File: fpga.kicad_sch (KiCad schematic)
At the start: 32 parts, among them J301 program, U301 ICE40HX8K-BG121, U302 W25Q32JVSS, Y301 50Mhz, Y302 12Mhz

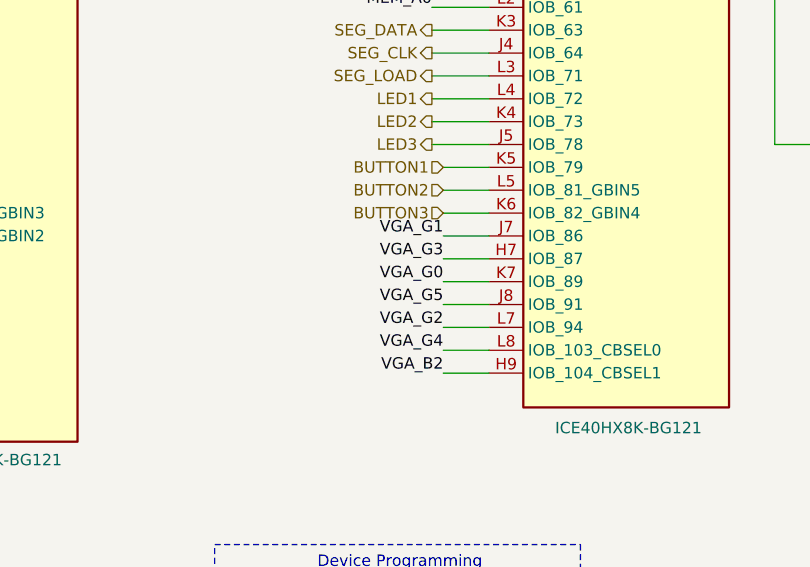
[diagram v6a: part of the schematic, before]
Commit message: Additional routing
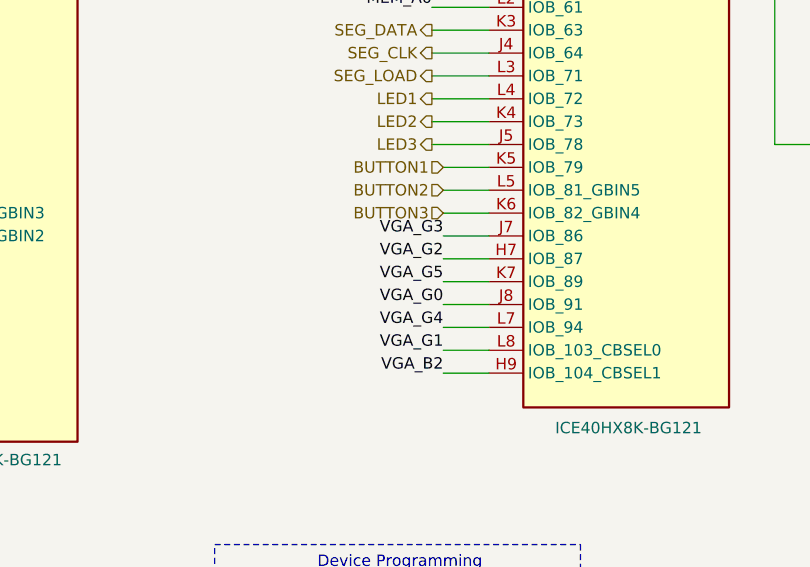
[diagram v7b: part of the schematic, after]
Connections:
- net VGA_G0: now also U301.J8 (IOB_91); no longer U301.K7 (IOB_89)
- net VGA_G1: now also U301.L8 (IOB_103_CBSEL0); no longer U301.J7 (IOB_86)
- net VGA_G2: now also U301.H7 (IOB_87); no longer U301.L7 (IOB_94)
- net VGA_G3: now also U301.J7 (IOB_86); no longer U301.H7 (IOB_87)
- net VGA_G4: now also U301.L7 (IOB_94); no longer U301.L8 (IOB_103_CBSEL0)
- net VGA_G5: now also U301.K7 (IOB_89); no longer U301.J8 (IOB_91)
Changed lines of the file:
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@@
 	)
 	(label "VGA_G5"
-		(at 166.37 78.74 180)
+		(at 166.37 76.2 180)
 		(effects
 			(font
@@
 	)
 	(label "VGA_G4"
-		(at 166.37 83.82 180)
+		(at 166.37 81.28 180)
 		(effects
 			(font
@@
 	)
 	(label "VGA_G0"
-		(at 166.37 76.2 180)
+		(at 166.37 78.74 180)
 		(effects
 			(font
@@
 	)
 	(label "VGA_G2"
-		(at 166.37 81.28 180)
+		(at 166.37 73.66 180)
 		(effects
 			(font
@@
 	)
 	(label "VGA_G3"
-		(at 166.37 73.66 180)
+		(at 166.37 71.12 180)
 		(effects
 			(font
@@
 	)
 	(label "VGA_G1"
-		(at 166.37 71.12 180)
-		(effects
-			(font
+		(at 166.37 83.82 180)
+		(effects
+			(font

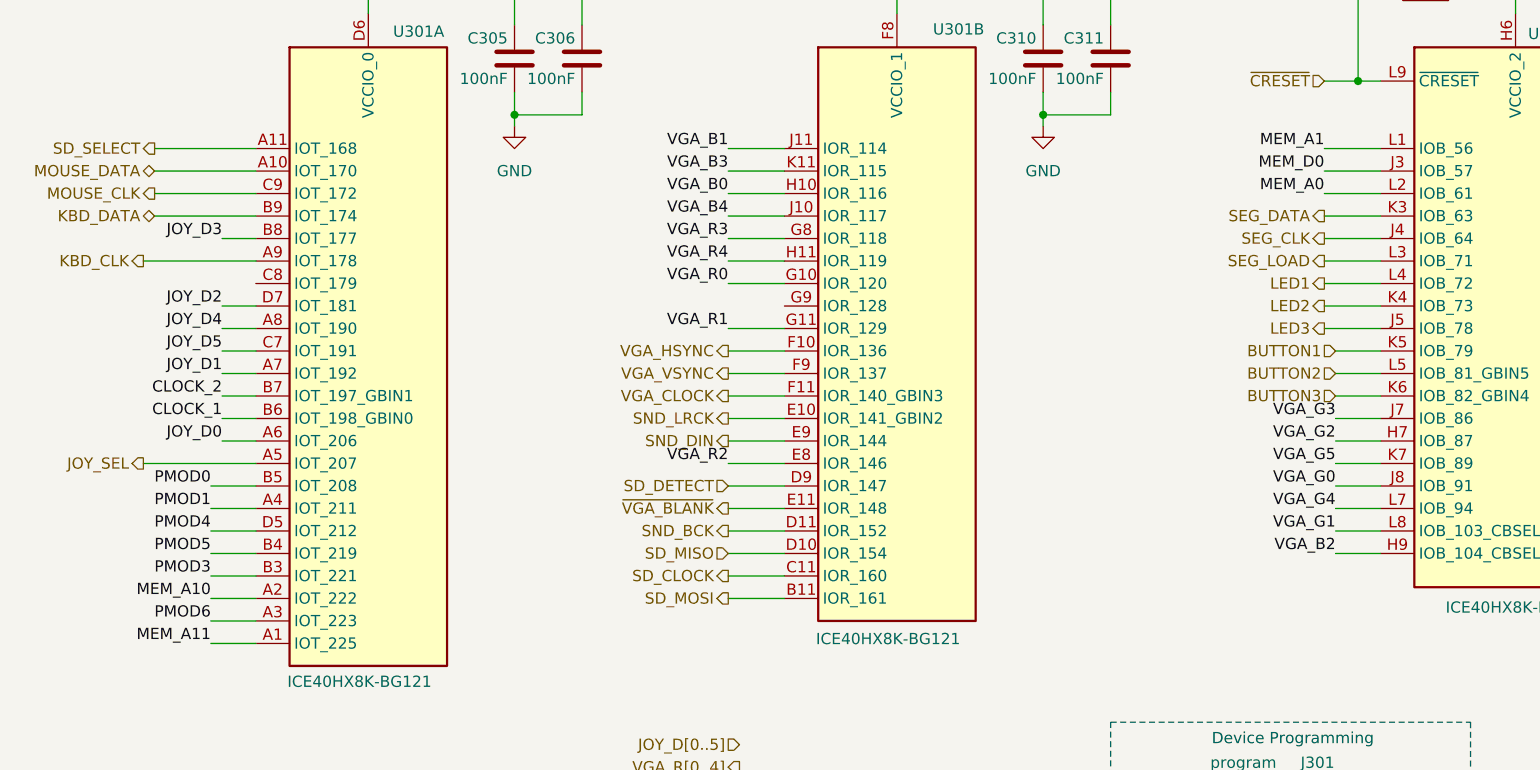
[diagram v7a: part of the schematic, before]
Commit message: More layout done
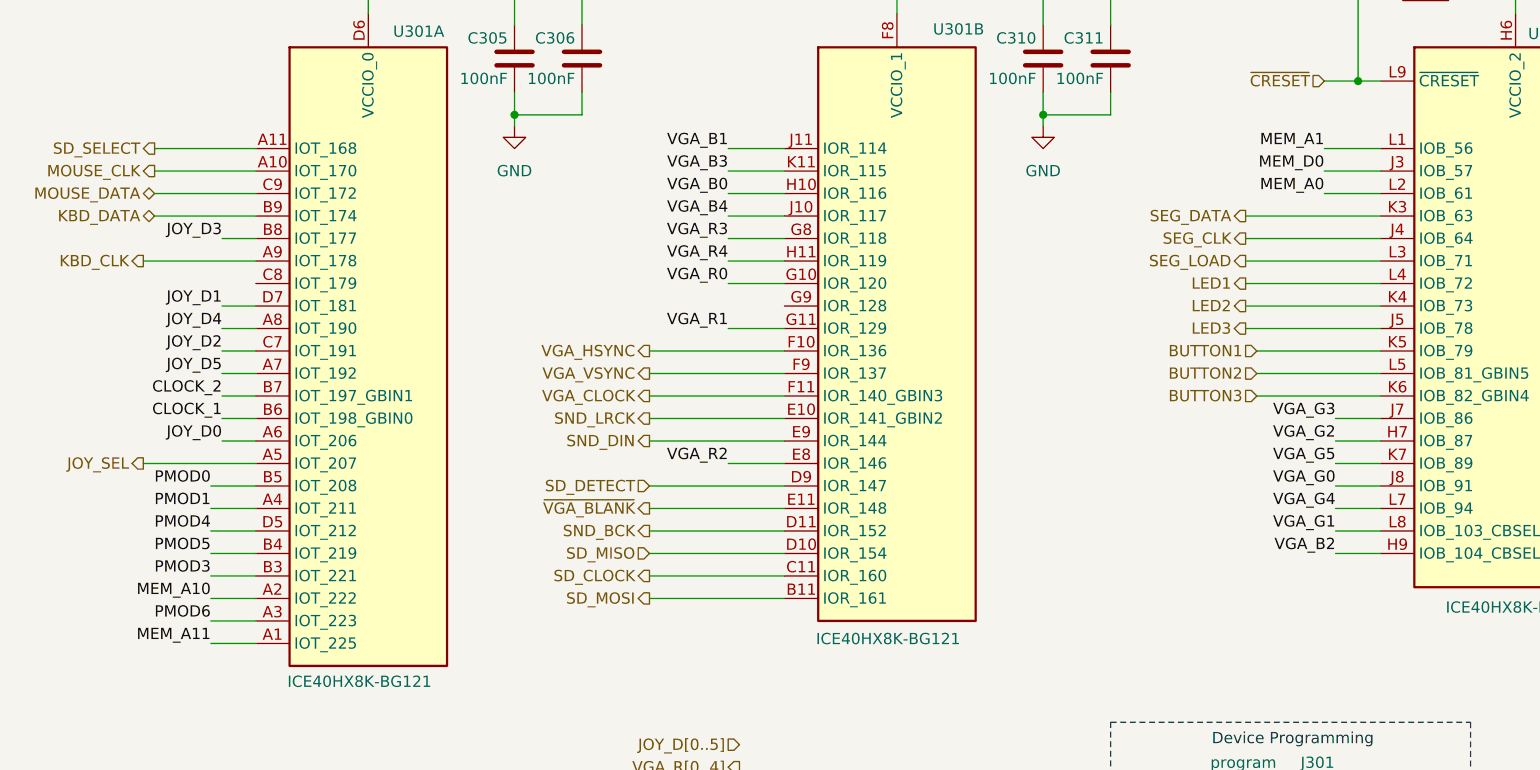
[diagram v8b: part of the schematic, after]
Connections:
- net JOY_D1: now also U301.D7 (IOT_181); no longer U301.A7 (IOT_192)
- net JOY_D2: now also U301.C7 (IOT_191); no longer U301.D7 (IOT_181)
- net JOY_D5: now also U301.A7 (IOT_192); no longer U301.C7 (IOT_191)
- net MOUSE_CLK: now also U301.A10 (IOT_170); no longer U301.C9 (IOT_172)
- net MOUSE_DATA: now also U301.C9 (IOT_172); no longer U301.A10 (IOT_170)
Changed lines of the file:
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@@
 	(wire
 		(pts
-			(xy 97.79 68.58) (xy 104.14 68.58)
+			(xy 88.9 68.58) (xy 104.14 68.58)
 		)
 		(stroke
@@
 	(wire
 		(pts
-			(xy 97.79 86.36) (xy 104.14 86.36)
+			(xy 88.9 86.36) (xy 104.14 86.36)
 		)
 		(stroke
@@
 	(wire
 		(pts
-			(xy 97.79 78.74) (xy 104.14 78.74)
+			(xy 88.9 78.74) (xy 104.14 78.74)
 		)
 		(stroke
@@
 	(wire
 		(pts
-			(xy 97.79 71.12) (xy 104.14 71.12)
+			(xy 88.9 71.12) (xy 104.14 71.12)
 		)
 		(stroke
@@
 	(wire
 		(pts
-			(xy 97.79 66.04) (xy 104.14 66.04)
+			(xy 88.9 66.04) (xy 104.14 66.04)
 		)
 		(stroke
@@
 	(wire
 		(pts
-			(xy 165.1 58.42) (xy 171.45 58.42)
+			(xy 156.21 58.42) (xy 171.45 58.42)
 		)
 		(stroke
@@
 	(wire
 		(pts
-			(xy 165.1 60.96) (xy 171.45 60.96)
+			(xy 156.21 60.96) (xy 171.45 60.96)
 		)
 		(stroke
@@
 	(wire
 		(pts
-			(xy 97.79 81.28) (xy 104.14 81.28)
+			(xy 88.9 81.28) (xy 104.14 81.28)
 		)
 		(stroke
@@
 	(wire
 		(pts
-			(xy 166.37 68.58) (xy 171.45 68.58)
+			(xy 157.48 68.58) (xy 171.45 68.58)
 		)
 		(stroke
@@
 	(wire
 		(pts
-			(xy 97.79 73.66) (xy 104.14 73.66)
+			(xy 88.9 73.66) (xy 104.14 73.66)
 		)
 		(stroke
@@
 	(wire
 		(pts
-			(xy 166.37 63.5) (xy 171.45 63.5)
+			(xy 157.48 63.5) (xy 171.45 63.5)
 		)
 		(stroke
@@
 	(wire
 		(pts
-			(xy 97.79 83.82) (xy 104.14 83.82)
+			(xy 88.9 83.82) (xy 104.14 83.82)
 		)
 		(stroke
@@
 	(wire
 		(pts
-			(xy 165.1 48.26) (xy 171.45 48.26)
+			(xy 156.21 48.26) (xy 171.45 48.26)
 		)
 		(stroke
@@
 	(wire
 		(pts
-			(xy 165.1 50.8) (xy 171.45 50.8)
+			(xy 156.21 50.8) (xy 171.45 50.8)
 		)
 		(stroke
@@
 	(wire
 		(pts
-			(xy 97.79 63.5) (xy 104.14 63.5)
+			(xy 88.9 63.5) (xy 104.14 63.5)
 		)
 		(stroke
@@
 	(wire
 		(pts
-			(xy 166.37 66.04) (xy 171.45 66.04)
+			(xy 157.48 66.04) (xy 171.45 66.04)
 		)
 		(stroke
@@
 	(wire
 		(pts
-			(xy 165.1 53.34) (xy 171.45 53.34)
+			(xy 156.21 53.34) (xy 171.45 53.34)
 		)
 		(stroke
@@
 	(wire
 		(pts
-			(xy 165.1 55.88) (xy 171.45 55.88)
+			(xy 156.21 55.88) (xy 171.45 55.88)
 		)
 		(stroke
@@
 	(wire
 		(pts
-			(xy 97.79 88.9) (xy 104.14 88.9)
+			(xy 88.9 88.9) (xy 104.14 88.9)
 		)
 		(stroke
@@
 	(wire
 		(pts
-			(xy 97.79 91.44) (xy 104.14 91.44)
+			(xy 88.9 91.44) (xy 104.14 91.44)
 		)
 		(stroke
@@
 	)
 	(label "JOY_D2"
-		(at 40.64 58.42 180)
+		(at 40.64 63.5 180)
 		(effects
 			(font
@@
 	)
 	(label "JOY_D5"
-		(at 40.64 63.5 180)
+		(at 40.64 66.04 180)
 		(effects
 			(font
@@
 	)
 	(label "JOY_D1"
-		(at 40.64 66.04 180)
+		(at 40.64 58.42 180)
 		(effects
 			(font
@@
 	(hierarchical_label "LED1"
 		(shape output)
-		(at 165.1 55.88 180)
+		(at 156.21 55.88 180)
 		(effects
 			(font
@@
 	(hierarchical_label "VGA_CLOCK"
 		(shape output)
-		(at 97.79 68.58 180)
+		(at 88.9 68.58 180)
 		(effects
 			(font
@@
 	(hierarchical_label "SD_CLOCK"
 		(shape output)
-		(at 97.79 88.9 180)
+		(at 88.9 88.9 180)
 		(effects
 			(font
@@
 	(hierarchical_label "SD_MOSI"
 		(shape output)
-		(at 97.79 91.44 180)
+		(at 88.9 91.44 180)
 		(effects
 			(font
@@
 	(hierarchical_label "~{VGA_BLANK}"
 		(shape output)
-		(at 97.79 81.28 180)
+		(at 88.9 81.28 180)
 		(effects
 			(font
@@
 	(hierarchical_label "VGA_HSYNC"
 		(shape output)
-		(at 97.79 63.5 180)
+		(at 88.9 63.5 180)
 		(effects
 			(font
@@
 	(hierarchical_label "SND_DIN"
 		(shape output)
-		(at 97.79 73.66 180)
+		(at 88.9 73.66 180)
 		(effects
 			(font
@@
 	(hierarchical_label "MOUSE_CLK"
 		(shape output)
-		(at 33.02 45.72 180)
+		(at 33.02 43.18 180)
 		(effects
 			(font
@@
 	(hierarchical_label "BUTTON1"
 		(shape input)
-		(at 166.37 63.5 180)
+		(at 157.48 63.5 180)
 		(effects
 			(font
@@
 	(hierarchical_label "LED2"
 		(shape output)
-		(at 165.1 58.42 180)
+		(at 156.21 58.42 180)
 		(effects
 			(font
@@
 	(hierarchical_label "SND_LRCK"
 		(shape output)
-		(at 97.79 71.12 180)
+		(at 88.9 71.12 180)
 		(effects
 			(font
@@
 	(hierarchical_label "SEG_DATA"
 		(shape output)
-		(at 165.1 48.26 180)
+		(at 156.21 48.26 180)
 		(effects
 			(font
@@
 	(hierarchical_label "SEG_LOAD"
 		(shape output)
-		(at 165.1 53.34 180)
+		(at 156.21 53.34 180)
 		(effects
 			(font
@@
 	(hierarchical_label "BUTTON3"
 		(shape input)
-		(at 166.37 68.58 180)
+		(at 157.48 68.58 180)
 		(effects
 			(font
@@
 	(hierarchical_label "LED3"
 		(shape output)
-		(at 165.1 60.96 180)
+		(at 156.21 60.96 180)
 		(effects
 			(font
@@
 	(hierarchical_label "SD_MISO"
 		(shape input)
-		(at 97.79 86.36 180)
+		(at 88.9 86.36 180)
 		(effects
 			(font
@@
 	(hierarchical_label "SEG_CLK"
 		(shape output)
-		(at 165.1 50.8 180)
+		(at 156.21 50.8 180)
 		(effects
 			(font
@@
 	(hierarchical_label "MOUSE_DATA"
 		(shape bidirectional)
-		(at 33.02 43.18 180)
+		(at 33.02 45.72 180)
 		(effects
 			(font
@@
 	(hierarchical_label "SD_DETECT"
 		(shape input)
-		(at 97.79 78.74 180)
+		(at 88.9 78.74 180)
 		(effects
 			(font
@@
 	(hierarchical_label "BUTTON2"
 		(shape input)
-		(at 166.37 66.04 180)
+		(at 157.48 66.04 180)
 		(effects
 			(font
@@
 	(hierarchical_label "SND_BCK"
 		(shape output)
-		(at 97.79 83.82 180)
+		(at 88.9 83.82 180)
 		(effects
 			(font
@@
 	(hierarchical_label "VGA_VSYNC"
 		(shape output)
-		(at 97.79 66.04 180)
+		(at 88.9 66.04 180)
 		(effects
 			(font
